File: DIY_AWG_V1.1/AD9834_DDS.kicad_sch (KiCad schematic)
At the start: 68 parts, among them IC2 ADG704BRMZ-REEL7, IC7 TLV3544IPWR, U10 AD9834, U13 HMC472ALP4ETR, U6 AMS1117-5.0, Y3 SG-615

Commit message: Updated AD9834_DDS and amplifier schematic
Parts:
- removed C68, C69, C80, C81, C82, C83, C84, C87: 100n, symbol Device:C
- removed C88, C89: 1u, symbol Device:C
- removed R44: 38.3, symbol Device:R
- removed R45: 11.5, symbol Device:R
- removed U13: HMC472ALP4ETR, easyeda2kicad:QFN-24_L4.0-W4.0-P0.50-TL-EP2.7, symbol easyeda2kicad:HMC472ALP4ETR
- added R55: 40.2, symbol Device:R
- added R56: 9.53, symbol Device:R
- added TP5: TestPoint, symbol Connector:TestPoint
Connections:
- net GND: now also R56.1
- net WAVE1_OUT: now also R55.2, R56.2
- net DC_OFFSET: now reaches IC7.9 (-IN_C), R53.2, R54.1
- net DC_OFFSET: now also TP5.1
- net +VSW5V0 renamed +VSW12V0
- net ATT_CONN: no longer names the net of C66.2, L12.1
- net ATT_CONN: now also R55.1
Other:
- note added: "1. Add single-channel opamp for producing DC_OFFSET signal 2. Produce DC_OFFSET signal ranging from -1.65V to 1.65V 3. Connect the DC_OFFSET signal to the gain input of the THS3091"
- note added: "A: Custom Waveform from STM32 DAC B: Sine Waveform from AD9834 C: DC Gain for LMH6505 D: DC Offset"
- note added: "Pending Check for Channel C"
- note removed: "1. Change IC1 to TLV3544 2. Add unity gain buffer opamp for introducing the DC gain 3. Add unity gain buffer opamp at output of VOUT 4. Add LPF at output of DAC1 to smoothen output waveform 5. Add Pi-Pad attenuator IC to ensure 50 ohm termination"
- note removed: "Attenuator"
- note removed: "Pin 25 is thermal pad"
- note removed: "Step down 3.3V to 0.6V"
- moved on the sheet: C66, C67, C70, C71, IC7, L12, R42, R43, R51, R52, R53, R54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

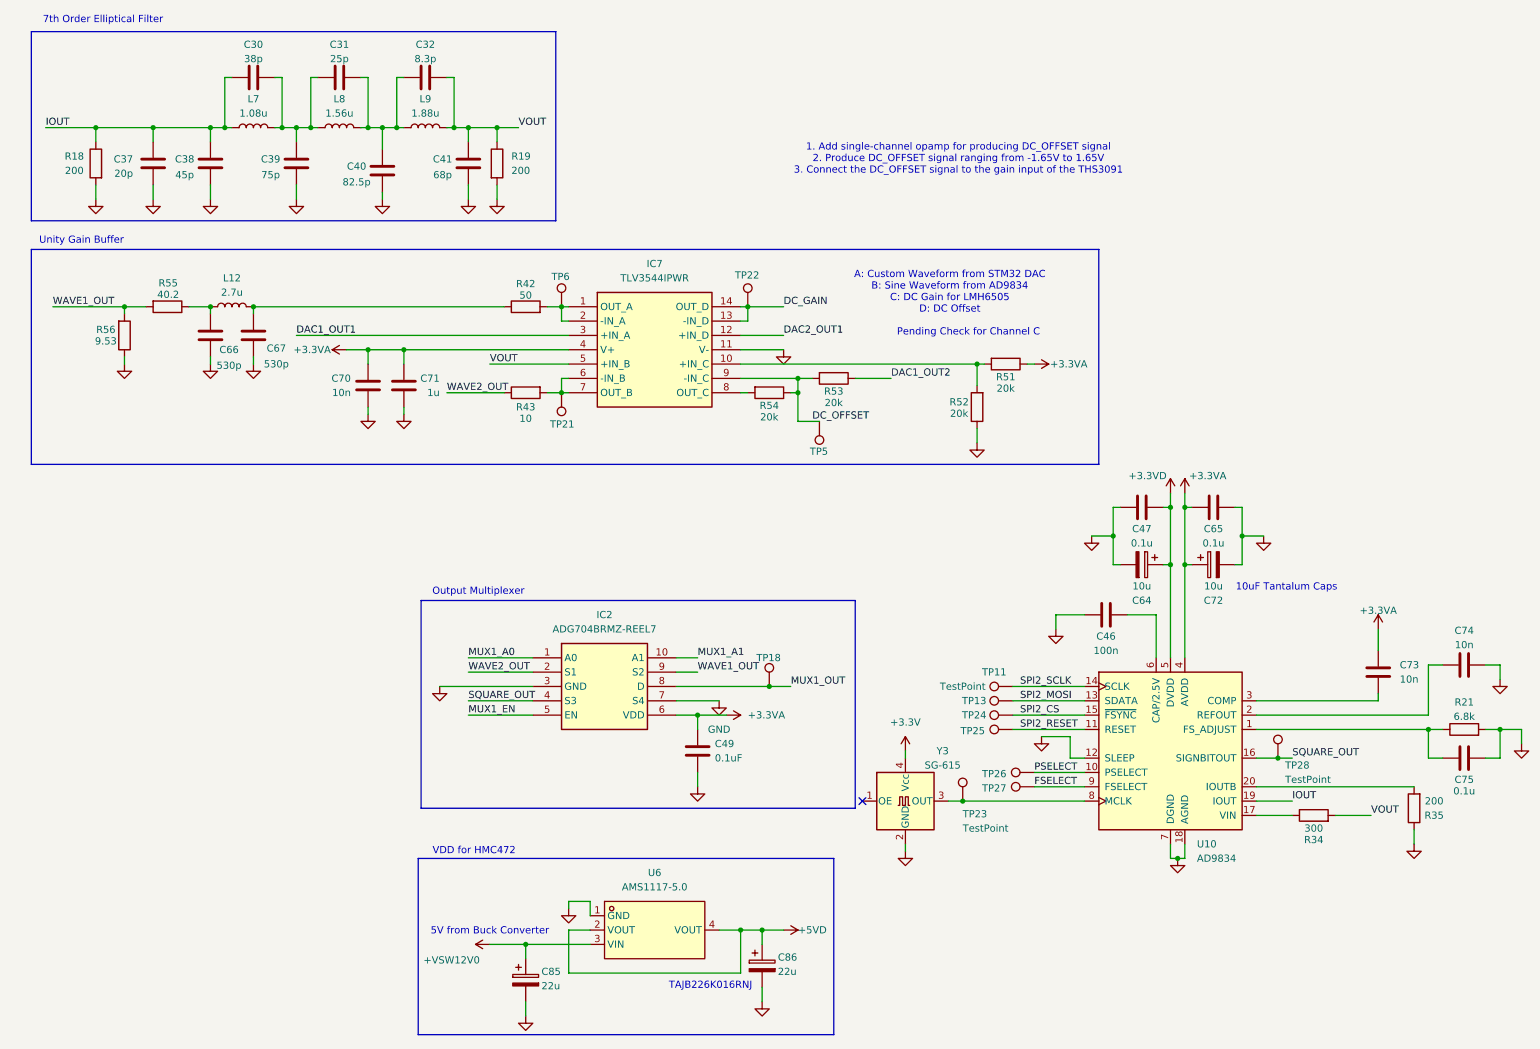
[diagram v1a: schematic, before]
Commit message: Updated AD9834_DDS, STM32_MCU, amplifier schematic
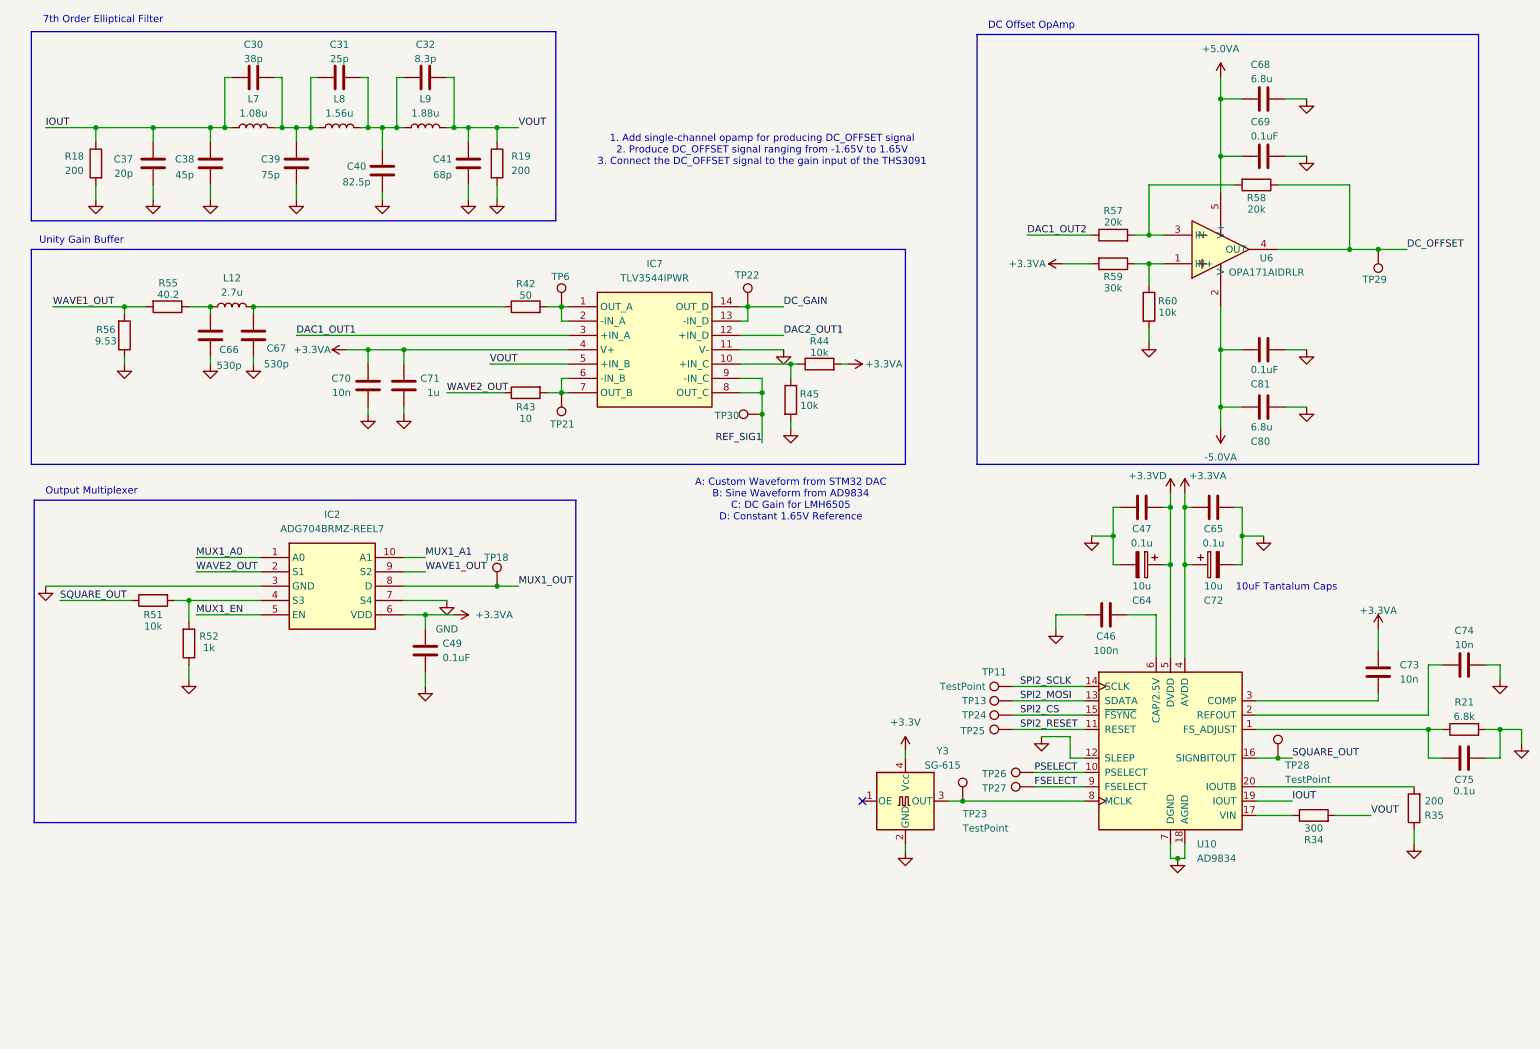
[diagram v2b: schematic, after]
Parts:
- removed C85, C86: 22u, symbol Device:C_Polarized
- removed R53, R54: 20k, symbol Device:R
- removed TP5: TestPoint, symbol Connector:TestPoint
- removed U6: AMS1117-5.0, easyeda2kicad:SOT-223_L6.5-W3.5-P2.30-LS7.0-BR, symbol easyeda2kicad:AMS1117-5.0
- added C68, C80: 6.8u, symbol Device:C
- added C69, C81: 0.1uF, symbol Device:C
- added R44, R45, R60: 10k, symbol Device:R
- added R57, R58: 20k, symbol Device:R
- added R59: 30k, symbol Device:R
- added TP29, TP30: TestPoint, symbol Connector:TestPoint
- added U6: OPA171AIDRLR, easyeda2kicad:SOT-5X3-5_L1.6-W1.2-P0.50-LS1.6-BR, symbol easyeda2kicad:OPA171AIDRLR
- R51: value 20k -> 10k
- R52: value 20k -> 1k
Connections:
- net +3.3VA: now also R44.2, R59.2; no longer R51.1
- net DAC1_OUT2: now also R57.1
- net DC_OFFSET: now also R58.1, TP29.1, U6.4 (OUT); no longer IC7.9 (-IN_C)
- net GND: now also C68.2, C69.2, C80.2, C81.2, R45.2, R60.2
- net SQUARE_OUT: now also R51.1; no longer IC2.4 (S3)
- net at R51.2, R52.2: now also IC2.4 (S3); no longer IC7.10 (+IN_C)
- net REF_SIG1: now reaches IC7.8 (OUT_C)
- net REF_SIG1: now also IC7.9 (-IN_C), TP30.1
- new net: R57.2, R58.2, U6.3 (IN-)
- new net: R59.1, R60.1, U6.1 (IN+)
- new net: IC7.10 (+IN_C), R44.1, R45.1
- new net +5.0VA: C68.1, C69.1, U6.5 (V+)
- new net -5.0VA: C80.1, C81.1, U6.2 (V-)
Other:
- note added: "A: Custom Waveform from STM32 DAC B: Sine Waveform from AD9834 C: DC Gain for LMH6505 D: Constant 1.65V Reference"
- note added: "DC Offset OpAmp"
- note removed: "5V from Buck Converter"
- note removed: "A: Custom Waveform from STM32 DAC B: Sine Waveform from AD9834 C: DC Gain for LMH6505 D: DC Offset"
- note removed: "Pending Check for Channel C"
- note removed: "TAJB226K016RNJ"
- note removed: "VDD for HMC472"
- moved on the sheet: C49, IC2, TP18

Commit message: Updated AD9834_DDS, amplifier schematic
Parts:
- R44: value 10k -> 20k
- R45: value 10k -> 1k
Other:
- note added: "A: Custom Waveform from STM32 DAC B: Sine Waveform from AD9834 C: DC Gain for LMH6505 D: Constant 0.157V Reference"
- note removed: "A: Custom Waveform from STM32 DAC B: Sine Waveform from AD9834 C: DC Gain for LMH6505 D: Constant 1.65V Reference"
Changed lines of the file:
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@@
 		)
 	)
-	(text "A: Custom Waveform from STM32 DAC\nB: Sine Waveform from AD9834\nC: DC Gain for LMH6505\nD: Constant 1.65V Reference"
+	(text "A: Custom Waveform from STM32 DAC\nB: Sine Waveform from AD9834\nC: DC Gain for LMH6505\nD: Constant 0.157V Reference"
 		(exclude_from_sim no)
 		(at 152.4 100.33 0)
@@
 			)
 		)
-		(property "Value" "10k"
+		(property "Value" "20k"
 			(at 157.48 74.168 90)
 			(show_name no)
@@
 			)
 		)
-		(property "Value" "10k"
+		(property "Value" "1k"
 			(at 155.702 83.566 0)
 			(show_name no)

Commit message: Updated AD9834_DDS, amplifier, STM32_MCU schematic
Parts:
- renumbered C37 to C35, C38 to C36, C66 to C37, C30 to C38, C67 to C39, C39 to C40, C31 to C41, C70 to C42, C40 to C43, C71 to C44, C32 to C45, C49 to C46, C41 to C47, C46 to C48, C47 to C49, C64 to C50, C65 to C51, C72 to C52, C68 to C53, C69 to C54, C81 to C55, C80 to C56, C73 to C57, C74 to C58, C75 to C59, IC2 to IC1, IC7 to IC2, L8 to L10, L9 to L11, L12 to L8, L7 to L9, R18 to R20, R56 to R21, R51 to R22, R55 to R23, R52 to R24, R19 to R25, R42 to R26, R43 to R27, R45 to R28, R44 to R29, R57 to R30, R59 to R31, R60 to R32, R58 to R33, R21 to R36, TP21 to TP10, TP22 to TP11, TP30 to TP12, TP23 to TP13, TP11 to TP14, TP13 to TP15, TP24 to TP16, TP25 to TP17, TP26 to TP18, TP27 to TP19, TP28 to TP20, TP29 to TP21, TP18 to TP8, TP6 to TP9, U10 to U11, U6 to U12, Y3 to Y2

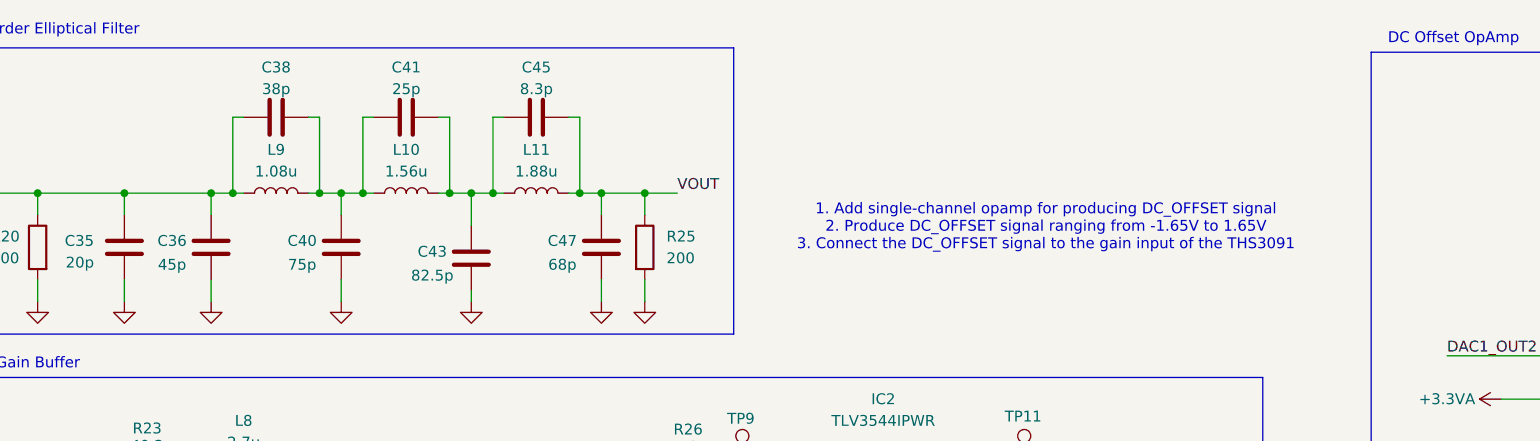
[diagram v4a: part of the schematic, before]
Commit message: Updated power_supply, AD9834_DDS schematic
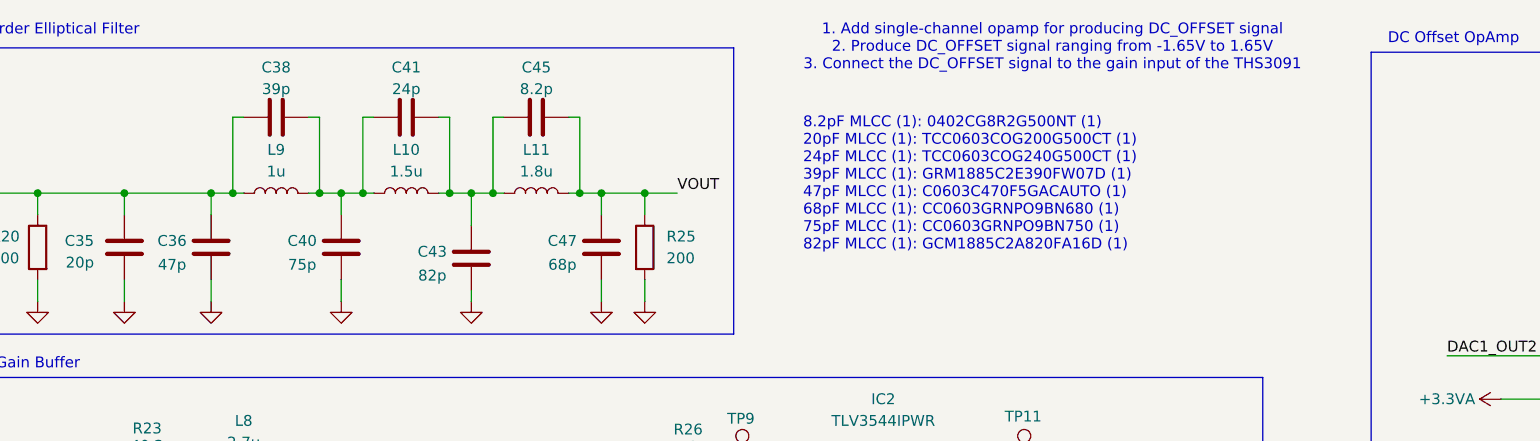
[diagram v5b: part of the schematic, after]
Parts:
- C36: value 45p -> 47p
- C38: value 38p -> 39p
- C41: value 25p -> 24p
- C43: value 82.5p -> 82p
- C45: value 8.3p -> 8.2p
- L10: value 1.56u -> 1.5u
- L11: value 1.88u -> 1.8u
- L9: value 1.08u -> 1u
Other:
- note added: "8.2pF MLCC (1): 0402CG8R2G500NT (1) 20pF MLCC (1): TCC0603COG200G500CT (1) 24pF MLCC (1): TCC0603COG240G500CT (1) 39pF MLCC (1): GRM1885C2E390FW07D (1) 47pF MLCC (1): C0603C470F5GACAUTO (1) 68pF MLCC (1): CC0603GRNPO9BN680 (1) 75pF MLCC (1): CC0603GRNPO9BN750 (1) 82pF MLCC (1): GCM1885C2A820FA16D (1)"
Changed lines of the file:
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@@
 		)
 	)
+	(text "8.2pF MLCC (1): 0402CG8R2G500NT (1)\n20pF MLCC (1): TCC0603COG200G500CT (1)\n24pF MLCC (1): TCC0603COG240G500CT (1)\n39pF MLCC (1): GRM1885C2E390FW07D (1)\n47pF MLCC (1): C0603C470F5GACAUTO (1)\n68pF MLCC (1): CC0603GRNPO9BN680 (1)\n75pF MLCC (1): CC0603GRNPO9BN750 (1)\n82pF MLCC (1): GCM1885C2A820FA16D (1)"
+		(exclude_from_sim no)
+		(at 118.872 33.274 0)
+		(effects
+			(font
+				(size 1.27 1.27)
+			)
+			(justify left)
+		)
+	)
 	(text "7th Order Elliptical Filter\n"
 		(exclude_from_sim no)
@@
 	(text "1. Add single-channel opamp for producing DC_OFFSET signal\n2. Produce DC_OFFSET signal ranging from -1.65V to 1.65V\n3. Connect the DC_OFFSET signal to the gain input of the THS3091"
 		(exclude_from_sim no)
-		(at 147.32 38.354 0)
+		(at 148.082 17.272 0)
 		(effects
 			(font
@@
 			)
 		)
-		(property "Value" "45p"
+		(property "Value" "47p"
 			(at 44.958 42.672 0)
 			(show_name no)
@@
 			)
 		)
-		(property "Value" "1.88u"
+		(property "Value" "1.8u"
 			(at 87.63 31.75 90)
 			(show_name no)
@@
 			)
 		)
-		(property "Value" "1.56u"
+		(property "Value" "1.5u"
 			(at 72.39 31.75 90)
 			(show_name no)
@@
 			)
 		)
-		(property "Value" "82.5p"
+		(property "Value" "82p"
 			(at 75.438 43.942 0)
 			(show_name no)
@@
 			)
 		)
-		(property "Value" "8.3p"
+		(property "Value" "8.2p"
 			(at 87.63 22.098 90)
 			(show_name no)
@@
 			)
 		)
-		(property "Value" "1.08u"
+		(property "Value" "1u"
 			(at 57.15 31.75 90)
 			(show_name no)
@@
 			)
 		)
-		(property "Value" "25p"
+		(property "Value" "24p"
 			(at 72.39 22.098 90)
 			(show_name no)
@@
 			)
 		)
-		(property "Value" "38p"
+		(property "Value" "39p"
 			(at 57.15 22.098 90)
 			(show_name no)
